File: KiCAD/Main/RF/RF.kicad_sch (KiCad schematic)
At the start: 4 parts, among them IC1 E22-900M22S

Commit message: post meeting update
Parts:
- removed C1: 100nF, ProDoc_Sch-easyedapro:C0603, symbol ProDoc_Sch-easyedapro:CAP
- removed E22-900T22S1: ~, ProLib_pcs_2025-11-10:WIRELM-SMD_E22-900T22S, symbol New_Library:E22-900T22S

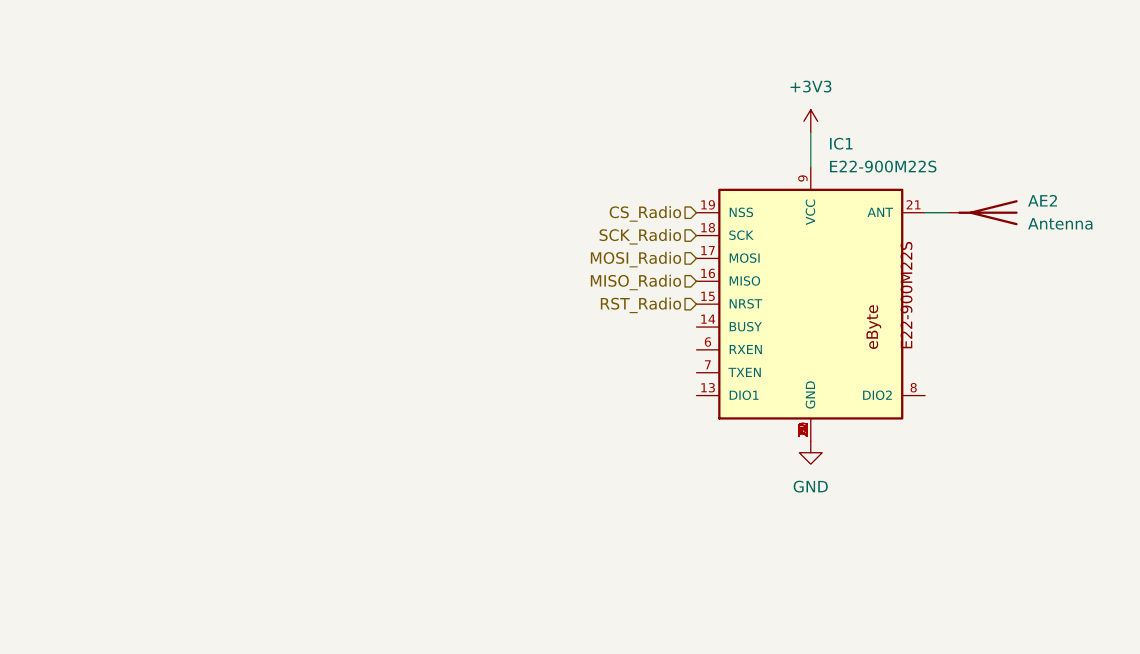
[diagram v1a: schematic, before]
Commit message: Remove thermocouples due to complexity and focus switch
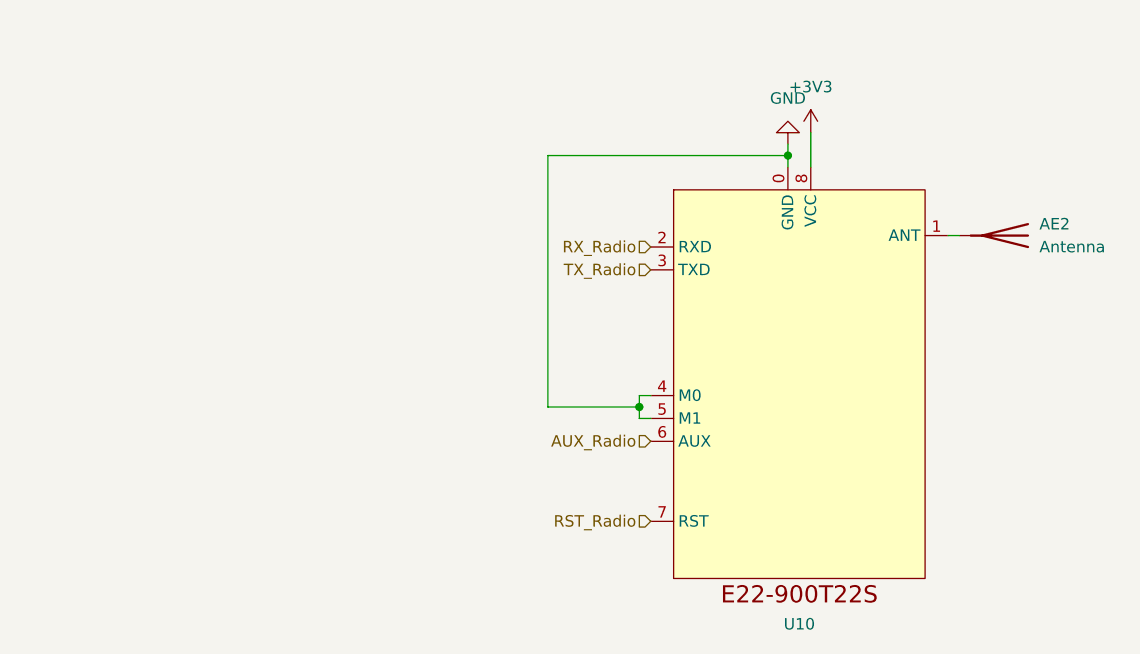
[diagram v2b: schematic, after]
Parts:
- removed IC1: E22-900M22S, E22-900M22S:E22-900M22S, symbol E22-900M22S:E22-900M22S
- added U10: ~, symbol E22-900T22S:E22-900T22S
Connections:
- net +3V3: now also U10.8 (VCC)
- net GND: now also U10.0 (GND), U10.4 (M0), U10.5 (M1)
- net RST_Radio: now also U10.7 (RST)
- net at AE2.1 (A): now also U10.1 (ANT)
- new net AUX_Radio: U10.6 (AUX)
- new net RX_Radio: U10.2 (RXD)
- new net TX_Radio: U10.3 (TXD)
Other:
- moved on the sheet: AE2
